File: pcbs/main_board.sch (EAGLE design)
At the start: 36 parts, among them IC1 317T, IC2 MEGA48/88/168-AU, J1 22-27-2021-02, K1 G6K-2F, Q1 MOSFET-NCHANNELSMD, Q2 MOSFET-NCHANNELSMD

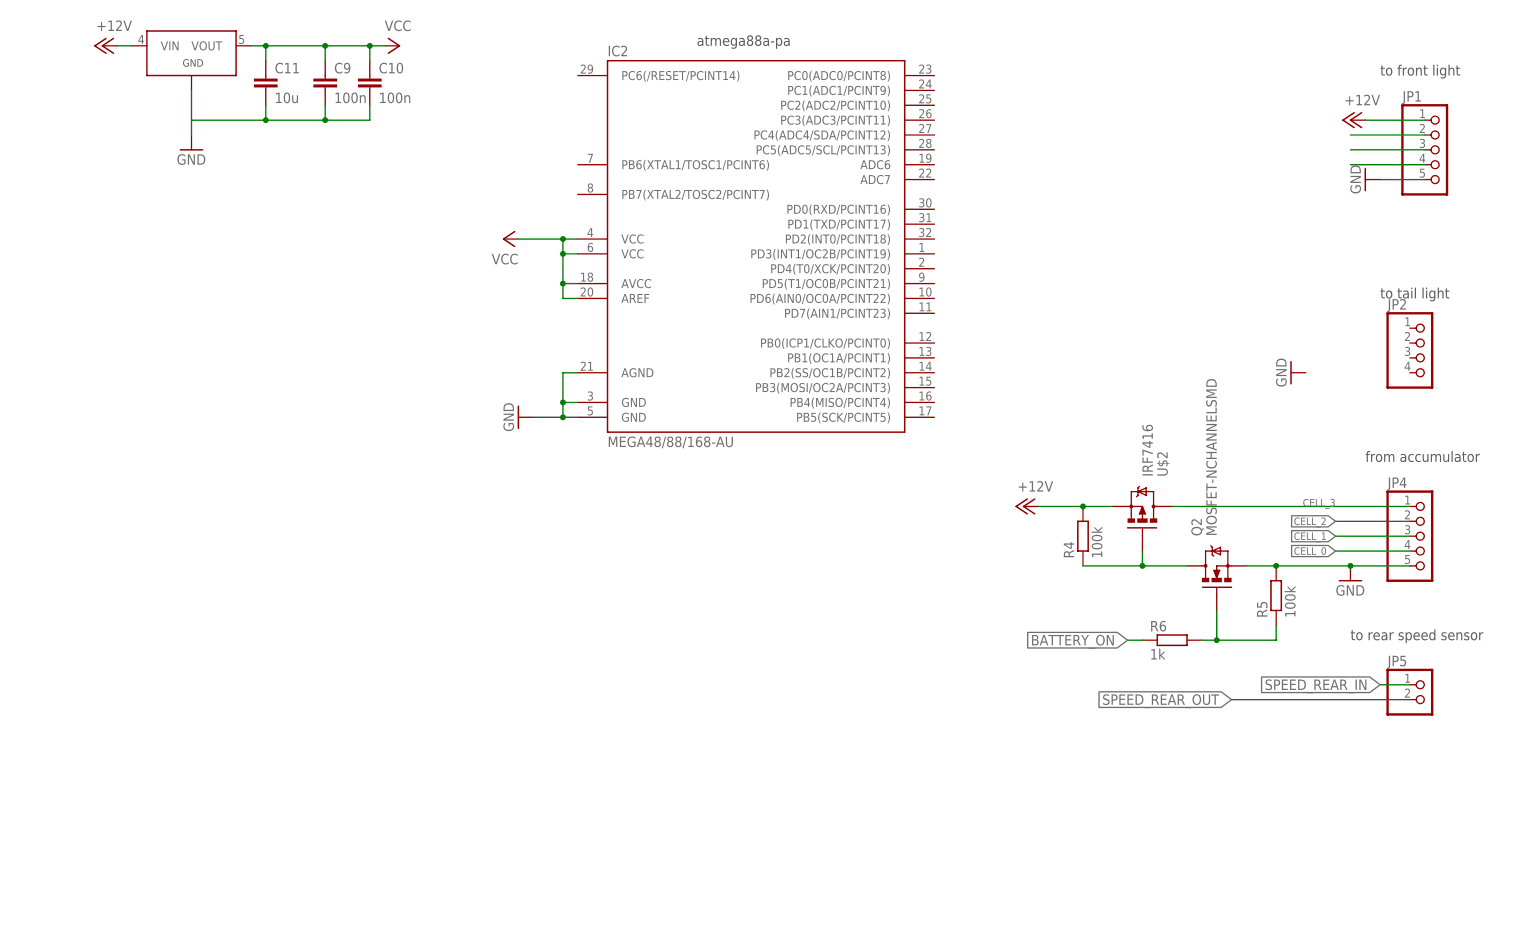
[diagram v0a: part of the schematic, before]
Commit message: Main Board: Added connections to front and to tail light.
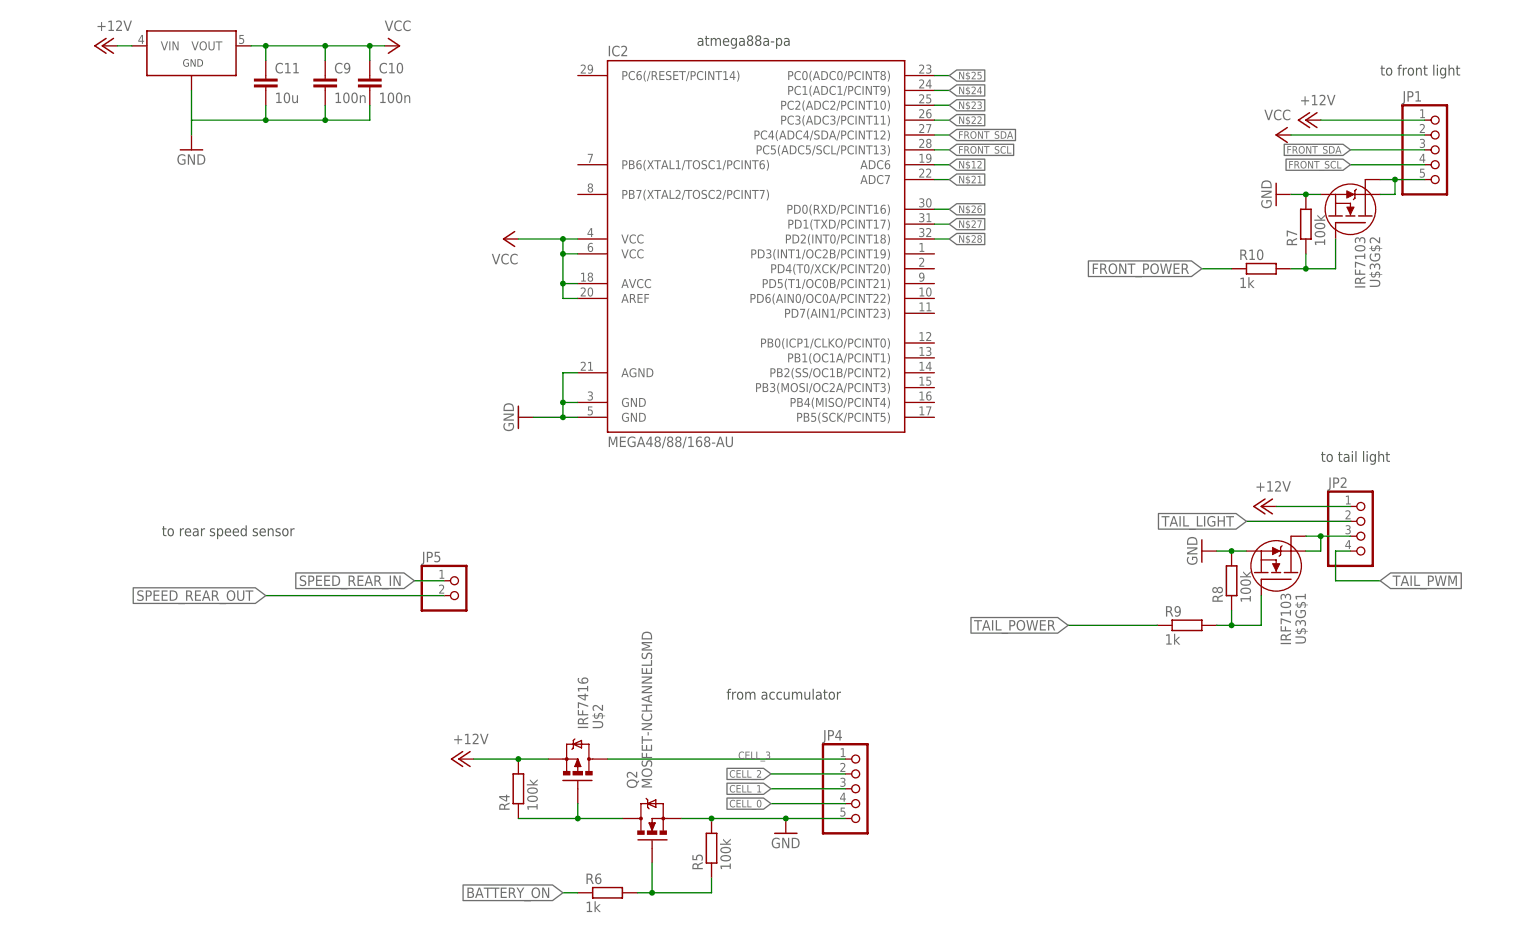
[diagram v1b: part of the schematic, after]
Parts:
- added R10, R9: 1k, resistor:R-EU_R0805
- added R7, R8: 100k, resistor:R-EU_R0805
- added U$3: IRF7103, irf-2:IRF7103
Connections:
- removed net N$11: JP1.3
- removed net N$7: JP1.2
- new net FRONT_POWER: R10.1
- new net FRONT_SCL: IC2.PC5(ADC5/SCL/PCINT13), JP1.4
- new net FRONT_SDA: IC2.PC4(ADC4/SDA/PCINT12), JP1.3
- new net N$13: JP1.5, U$3G$2.D@1, U$3G$2.D@2
- new net N$18: JP2.3, U$3G$1.D@1, U$3G$1.D@2
- new net N$19: R10.2, R7.1, U$3G$2.G
- new net N$20: R8.1, R9.2, U$3G$1.G
- new net N$21: IC2.ADC7
- new net N$22: IC2.PC3(ADC3/PCINT11)
- new net N$23: IC2.PC2(ADC2/PCINT10)
- new net N$24: IC2.PC1(ADC1/PCINT9)
- new net N$25: IC2.PC0(ADC0/PCINT8)
- new net N$26: IC2.PD0(RXD/PCINT16)
- new net N$27: IC2.PD1(TXD/PCINT17)
- new net N$28: IC2.PD2(INT0/PCINT18)
- new net TAIL_LIGHT: JP2.2
- new net TAIL_POWER: R9.1
- new net TAIL_PWM: JP2.4
- net +12V: now also JP2.1
- net GND: now also R7.2, R8.2, U$3G$1.S, U$3G$2.S; no longer JP1.5
- net N$12: now also IC2.ADC6; no longer JP1.4
- net VCC: now also JP1.2
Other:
- moved on the sheet: JP2, JP4, JP5, Q2, R4, R5, R6, U$2

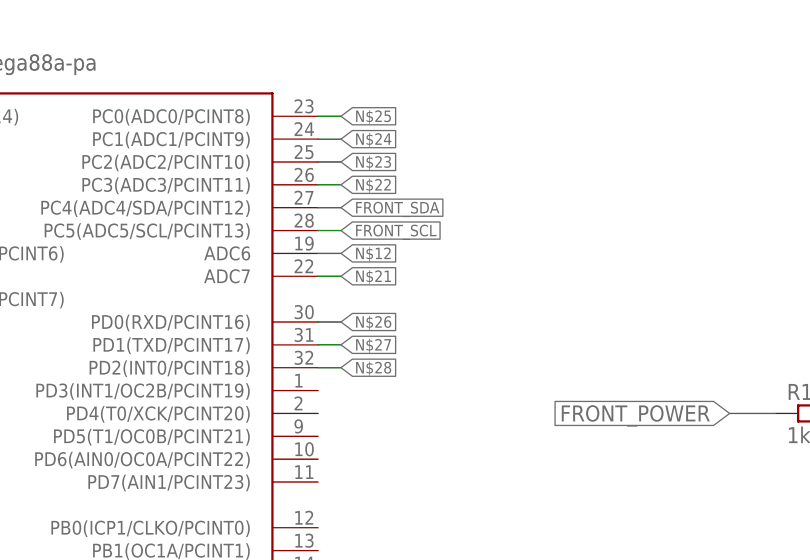
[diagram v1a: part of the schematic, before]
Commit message: Main Board: Changed fuse and corrected wrong connection.
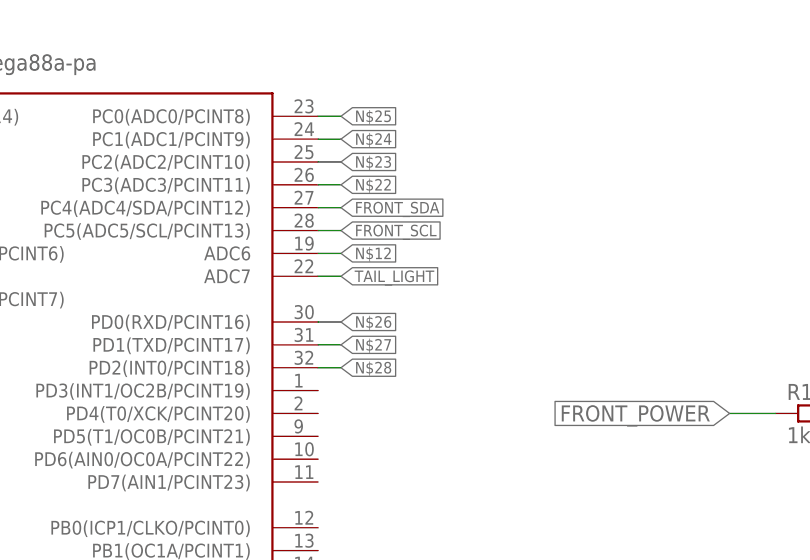
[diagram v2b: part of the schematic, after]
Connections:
- removed net N$21: IC2.ADC7
- net TAIL_LIGHT: now also IC2.ADC7
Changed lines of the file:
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@@
 <label x="469.9" y="81.28" size="1.778" layer="95" rot="MR0" xref="yes"/>
+</segment>
+<segment>
+<pinref part="IC2" gate="1" pin="ADC7"/>
+<wire x1="416.56" y1="139.7" x2="419.1" y2="139.7" width="0.1524" layer="91"/>
+<label x="419.1" y="139.7" size="1.27" layer="95" xref="yes"/>
 </segment>
 </net>
@@
 </segment>
 </net>
-<net name="N$21" class="0">
-<segment>
-<pinref part="IC2" gate="1" pin="ADC7"/>
-<wire x1="416.56" y1="139.7" x2="419.1" y2="139.7" width="0.1524" layer="91"/>
-<label x="419.1" y="139.7" size="1.27" layer="95" xref="yes"/>
-</segment>
-</net>

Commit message: Main Board: Added resistor dividers for voltage measurements.
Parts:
- added C12: 10n, resistor:C-EUC0805
- added JP3: AVR-ISP-6VERT, ShortCircuitRobotics:AVR-ISP-6VERT
- added R11, R12, R13, R14, R15, R16, R17, R18: 1k, resistor:R-EU_R0805
- added R19: 100k, resistor:R-EU_R0805
- F1: value FUSE19560 -> (none); device fuse:FUSE19560 -> fuse:TE5; OC_FARNELL (none) -> unknown; OC_NEWARK (none) -> unknown
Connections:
- removed net N$22: IC2.PC3(ADC3/PCINT11)
- removed net N$23: IC2.PC2(ADC2/PCINT10)
- removed net N$24: IC2.PC1(ADC1/PCINT9)
- removed net N$25: IC2.PC0(ADC0/PCINT8)
- removed net N$5: C3.+, C5.+, C6.+, C7.1, D2.C, D4.C, D5.2, IC1.VI, R1.2
- new net ADC0: IC2.PC0(ADC0/PCINT8), R11.2, R12.1
- new net ADC1: IC2.PC1(ADC1/PCINT9), R13.2, R14.1
- new net ADC2: IC2.PC2(ADC2/PCINT10), R15.2, R16.1
- new net ADC3: IC2.PC3(ADC3/PCINT11), R17.2, R18.1
- new net CELL3: R15.1
- new net N$11: C2.-, D3.C, D4.A
- new net N$21: IC2.PB3(MOSI/OC2A/PCINT3), JP3.4
- new net N$7: IC2.PB5(SCK/PCINT5), JP3.3
- new net RESET: IC2.PC6(/RESET/PCINT14), JP3.5
- new net V_IN: C3.+, C5.+, C6.+, C7.1, D2.C, D4.C, D5.2, IC1.VI, R1.2, R11.1
- net +12V: now also R13.1
- net BATTERY_ON: now also IC2.PB7(XTAL2/TOSC2/PCINT7)
- net FRONT_POWER: now also IC2.ADC6
- net GND: now also C12.2, JP3.6, R12.2, R14.2, R16.2, R18.2
- net INPUT_SEL: now also IC2.PB6(XTAL1/TOSC1/PCINT6)
- net N$1: now also K12.O, K13.O
- net N$12: now also IC2.PB4(MISO/PCINT4), JP3.1; no longer IC2.ADC6
- net N$2: now also C12.1, IC2.AREF; no longer C2.-, D3.C, D4.A, K12.O, K13.O
- net SPEED_REAR_IN: now also IC2.PD3(INT1/OC2B/PCINT19)
- net SPEED_REAR_OUT: now also IC2.PD4(T0/XCK/PCINT20)
- net TAIL_LIGHT: now also R19.2
- net TAIL_POWER: now also IC2.PB0(ICP1/CLKO/PCINT0)
- net TAIL_PWM: now also IC2.PD6(AIN0/OC0A/PCINT22)
- net VCC: now also JP3.2, R19.1; no longer IC2.AREF

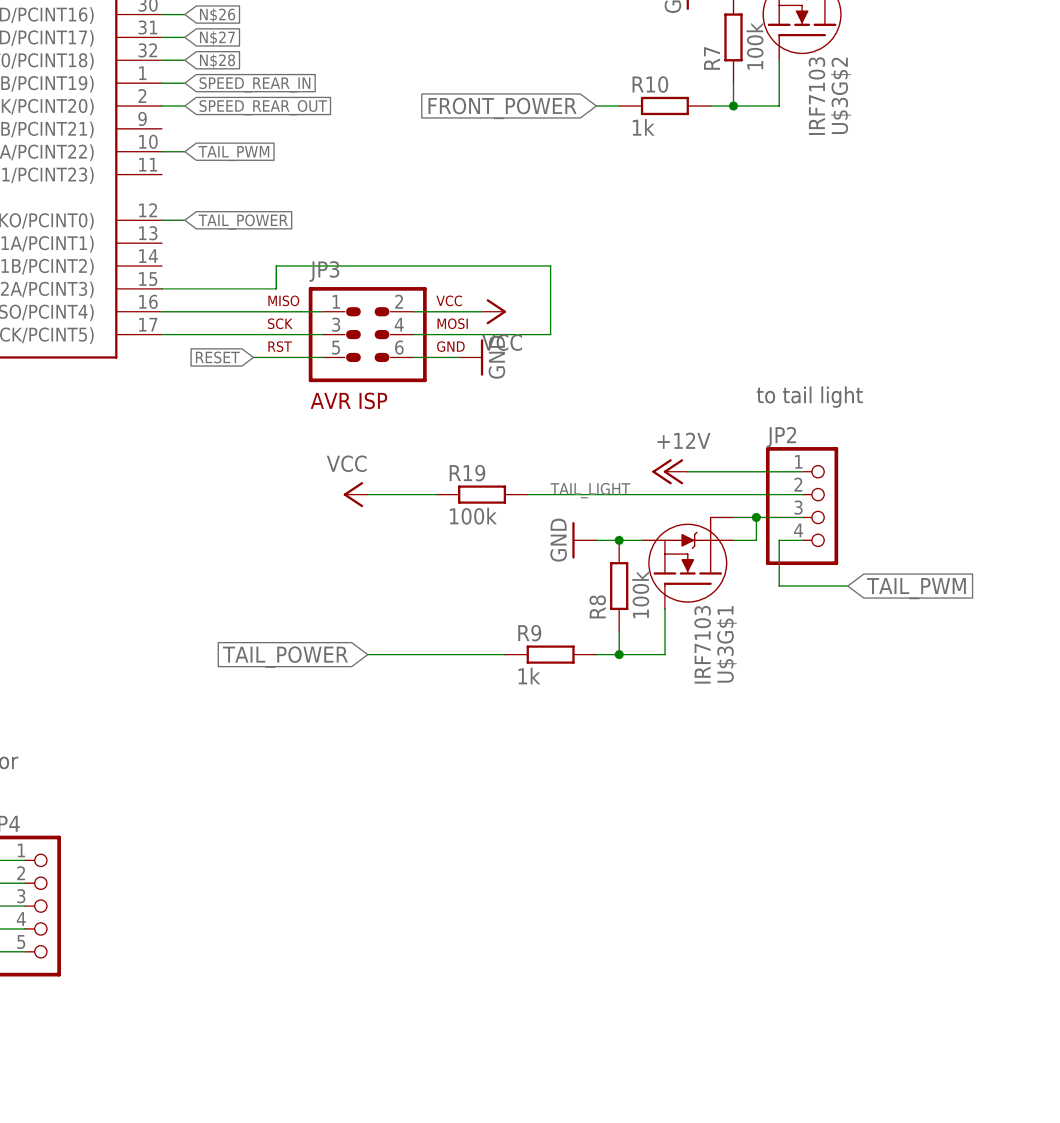
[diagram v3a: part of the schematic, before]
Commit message: Main Board: Added switchable 12V output.
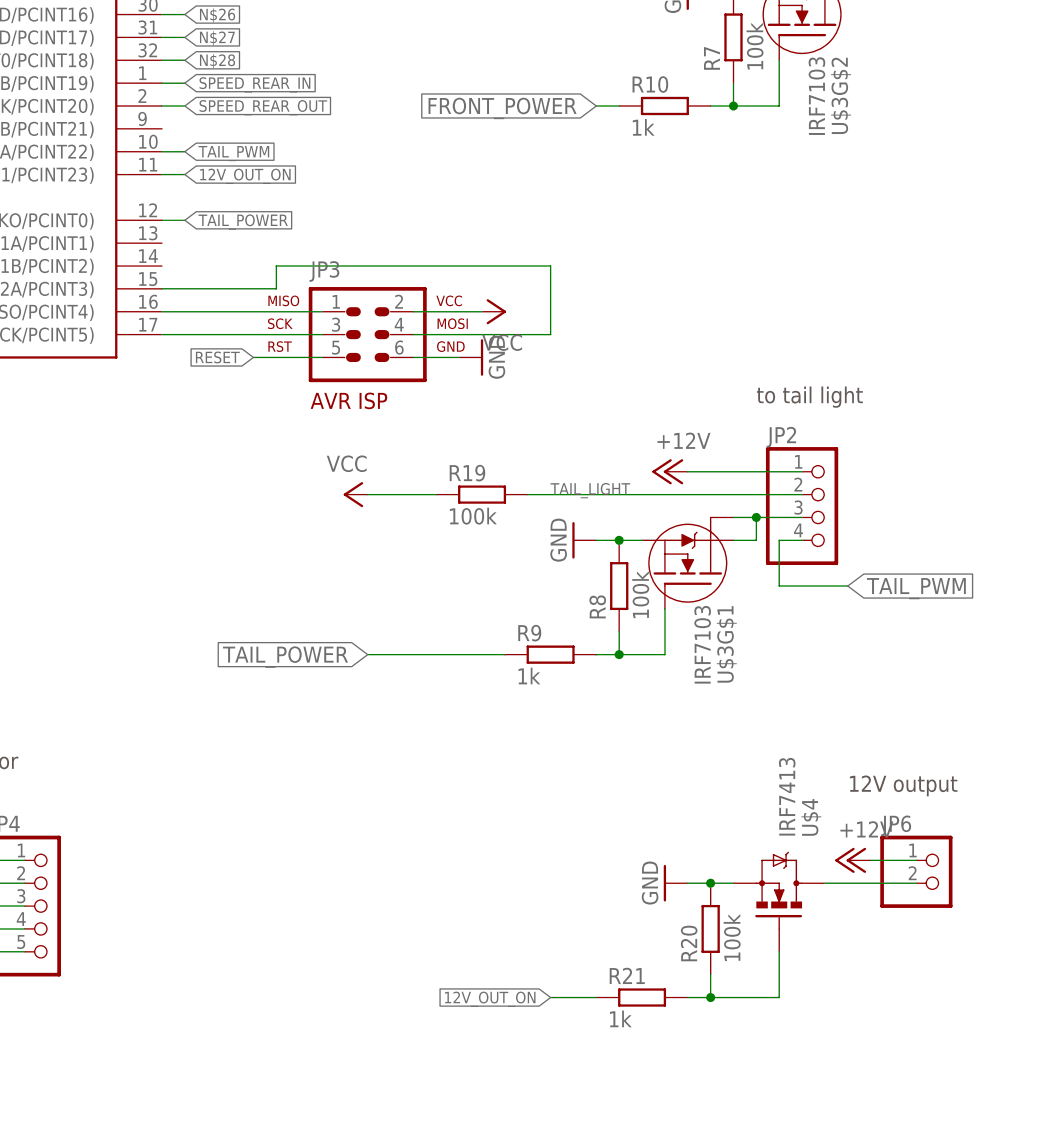
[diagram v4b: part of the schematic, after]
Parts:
- added JP6: (no value), pinhead:PINHD-1X2
- added R20: 100k, resistor:R-EU_R0805
- added R21: 1k, resistor:R-EU_R0805
- added U$4: IRF7413, ShortCircuitRobotics:IRF7413
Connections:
- new net 12V_OUT_ON: IC2.PD7(AIN1/PCINT23), R21.1
- new net N$22: R20.1, R21.2, U$4.G
- new net N$5: JP6.2, U$4.D1
- net +12V: now also JP6.1
- net GND: now also R20.2, U$4.S1
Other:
- note added: "12V output"
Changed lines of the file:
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@@
 <part name="P+12" library="supply1" deviceset="VCC" device=""/>
 <part name="R19" library="resistor" deviceset="R-EU_" device="R0805" value="100k"/>
+<part name="JP6" library="pinhead" deviceset="PINHD-1X2" device=""/>
+<part name="P+13" library="supply1" deviceset="+12V" device=""/>
+<part name="GND14" library="supply1" deviceset="GND" device=""/>
+<part name="R20" library="resistor" deviceset="R-EU_" device="R0805" value="100k"/>
+<part name="R21" library="resistor" deviceset="R-EU_" device="R0805" value="1k"/>
+<part name="U$4" library="ShortCircuitRobotics" deviceset="IRF7413" device=""/>
 </parts>
 <sheets>
@@
 <text x="381" y="50.8" size="1.778" layer="97">from accumulator</text>
 <text x="284.48" y="78.74" size="1.778" layer="97">to rear speed sensor</text>
+<text x="492.76" y="48.26" size="1.778" layer="97">12V output</text>
 </plain>
 <instances>
@@
 <instance part="P+12" gate="VCC" x="436.88" y="81.28" rot="MR270"/>
 <instance part="R19" gate="G$1" x="452.12" y="81.28"/>
+<instance part="JP6" gate="G$1" x="502.92" y="38.1"/>
+<instance part="P+13" gate="1" x="492.76" y="40.64" rot="MR270"/>
+<instance part="GND14" gate="1" x="472.44" y="38.1" rot="R270"/>
+<instance part="R20" gate="G$1" x="477.52" y="33.02" rot="R90"/>
+<instance part="R21" gate="G$1" x="469.9" y="25.4"/>
+<instance part="U$4" gate="G$1" x="485.14" y="38.1" rot="MR90"/>
 </instances>
 <busses>
@@
 <wire x1="172.72" y1="43.18" x2="170.18" y2="43.18" width="0.1524" layer="91"/>
 </segment>
+<segment>
+<pinref part="GND14" gate="1" pin="GND"/>
+<pinref part="U$4" gate="G$1" pin="S1"/>
+<wire x1="480.06" y1="38.1" x2="477.52" y2="38.1" width="0.1524" layer="91"/>
+<pinref part="R20" gate="G$1" pin="2"/>
+<wire x1="477.52" y1="38.1" x2="474.98" y2="38.1" width="0.1524" layer="91"/>
+<junction x="477.52" y="38.1"/>
+</segment>
 </net>
 <net name="N$6" class="0">
@@
 <pinref part="P+11" gate="1" pin="+12V"/>
 <wire x1="134.62" y1="58.42" x2="139.7" y2="58.42" width="0.1524" layer="91"/>
+</segment>
+<segment>
+<pinref part="JP6" gate="G$1" pin="1"/>
+<pinref part="P+13" gate="1" pin="+12V"/>
+<wire x1="495.3" y1="40.64" x2="500.38" y2="40.64" width="0.1524" layer="91"/>
 </segment>
 </net>
@@
 </segment>
 </net>
+<net name="N$5" class="0">
+<segment>
+<pinref part="JP6" gate="G$1" pin="2"/>
+<pinref part="U$4" gate="G$1" pin="D1"/>
+<wire x1="490.22" y1="38.1" x2="500.38" y2="38.1" width="0.1524" layer="91"/>
+</segment>
+</net>
+<net name="N$22" class="0">
+<segment>
+<pinref part="R21" gate="G$1" pin="2"/>
+<pinref part="R20" gate="G$1" pin="1"/>
+<wire x1="474.98" y1="25.4" x2="477.52" y2="25.4" width="0.1524" layer="91"/>
+<wire x1="477.52" y1="25.4" x2="477.52" y2="27.94" width="0.1524" layer="91"/>
+<pinref part="U$4" gate="G$1" pin="G"/>
+<wire x1="477.52" y1="25.4" x2="485.14" y2="25.4" width="0.1524" layer="91"/>
+<wire x1="485.14" y1="25.4" x2="485.14" y2="30.48" width="0.1524" layer="91"/>
+<junction x="477.52" y="25.4"/>
+</segment>
+</net>
+<net name="12V_OUT_ON" class="0">
+<segment>
+<pinref part="R21" gate="G$1" pin="1"/>
+<wire x1="464.82" y1="25.4" x2="459.74" y2="25.4" width="0.1524" layer="91"/>
+<label x="459.74" y="25.4" size="1.27" layer="95" rot="MR0" xref="yes"/>
+</segment>
+<segment>
+<pinref part="IC2" gate="1" pin="PD7(AIN1/PCINT23)"/>
+<wire x1="416.56" y1="116.84" x2="419.1" y2="116.84" width="0.1524" layer="91"/>
+<label x="419.1" y="116.84" size="1.27" layer="95" xref="yes"/>
+</segment>
+</net>
